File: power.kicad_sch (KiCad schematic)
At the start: 22 parts, among them IC2 MPM3833CGRH-Z, IC5 BQ24074RGTR, IC6 LP2985-30DBVR, U1 NC7SVU04P5X

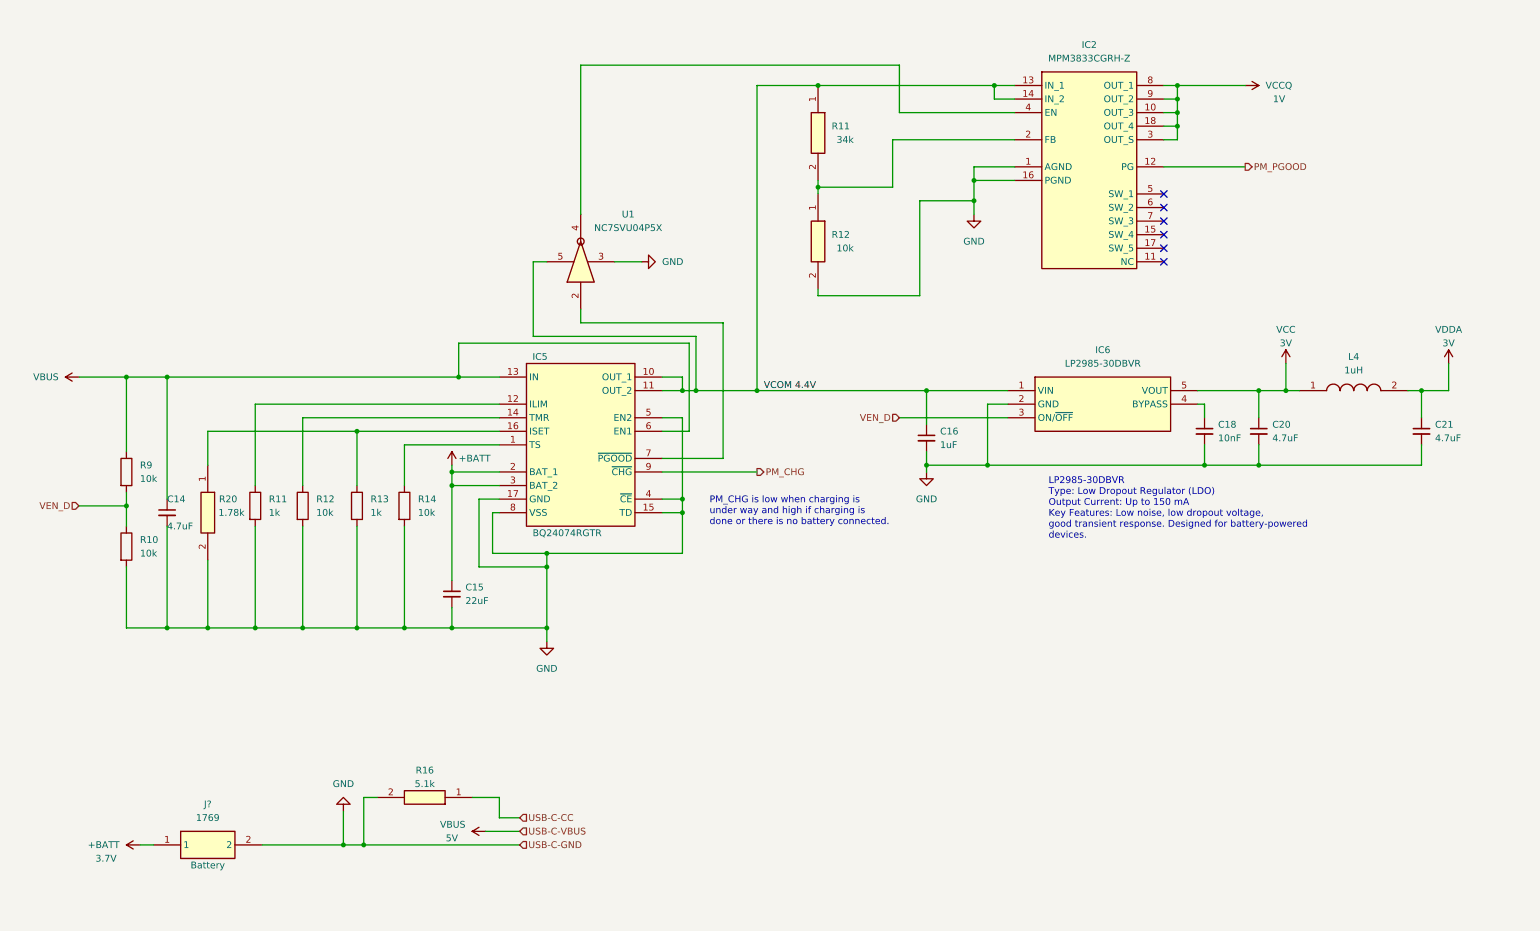
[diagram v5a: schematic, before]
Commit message: Rewired power module
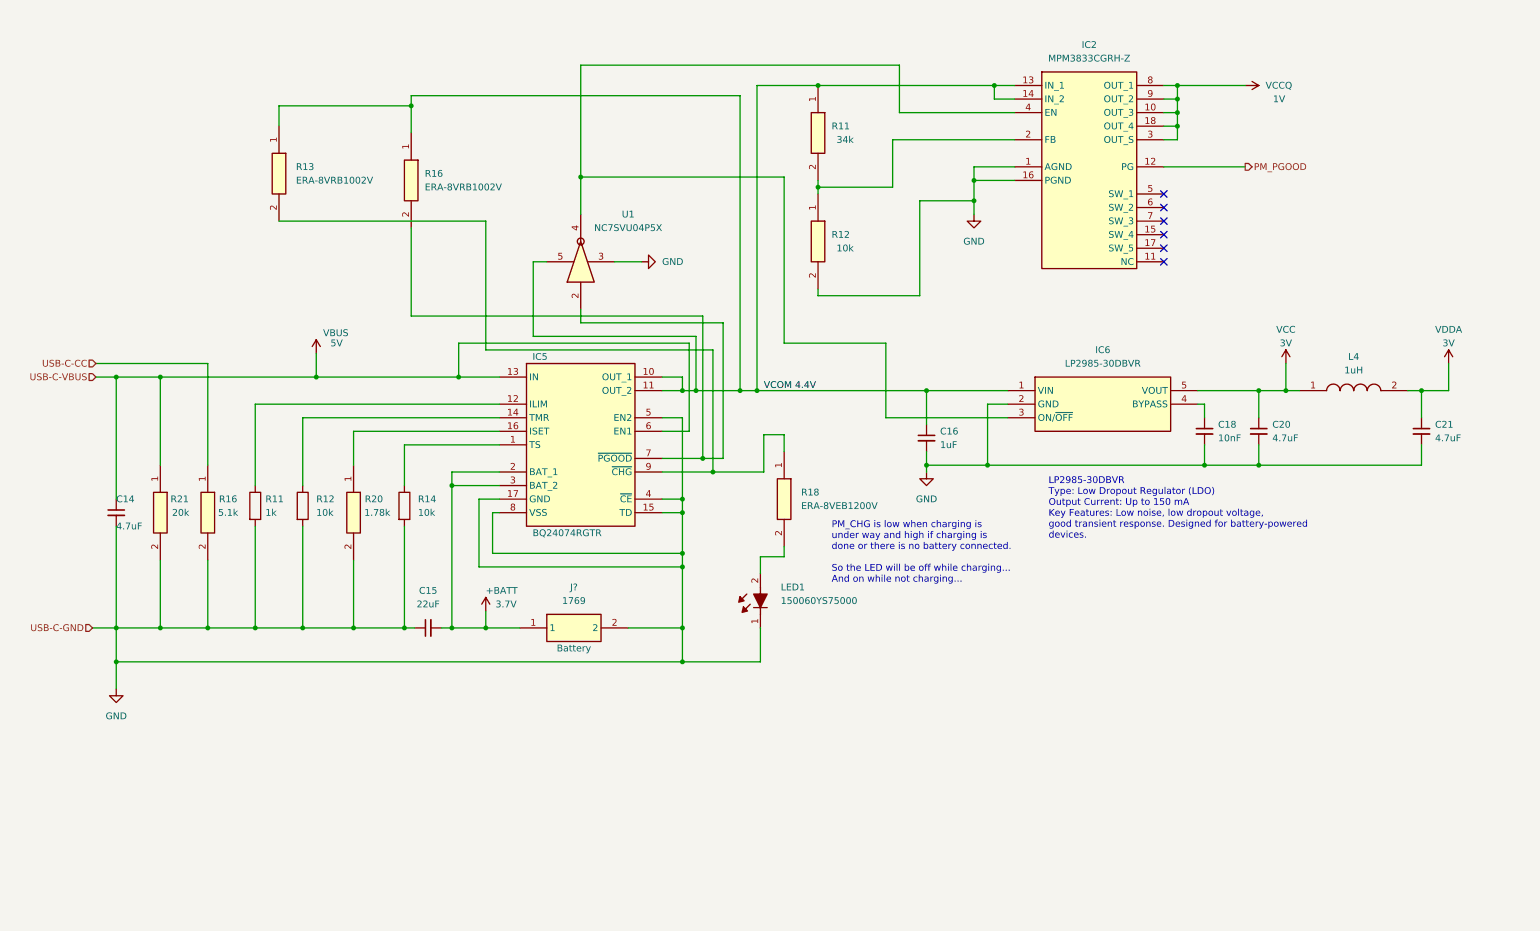
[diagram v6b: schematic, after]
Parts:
- removed R10, R9: 10k_0402, Resistor_SMD:R_0402_1005Metric, symbol PCM_4ms_Resistor:10k_0402
- removed R13: 1k_0603, 4ms_Resistor:R_0603, symbol PCM_4ms_Resistor:1k_0603
- added LED1: 150060YS75000, LEDC1608X80N, symbol SamacSys_Parts:150060YS75000
- added R13, R16: ERA-8VRB1002V, ERA8KEB1004V, symbol SamacSys_Parts:ERA-8VRB1002V
- added R18: ERA-8VEB1200V, ERA8KEB1004V, symbol SamacSys_Parts:ERA-8VEB1200V
- added R21: ERA-3VEB1781V, ERA3KV_(0603), symbol SamacSys_Parts:ERA-3VEB1781V
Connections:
- net VEN_D is gone; now on an unnamed net: IC6.3 (ON/~{OFF})
- net +BATT: now also C15.2; no longer C15.1
- net GND: now also C15.1, LED1.1 (K), R21.2; no longer C15.2
- net VBUS: now also R21.1
- net VCOM 4.4V: now also R13.1, R16.1
- net at IC5.7 (~{PGOOD}), U1.2: now also R16.2
- net PM_CHG: no longer names the net of IC5.9 (~{CHG})
- net PM_CHG: now also R13.2, R18.1
- new net: LED1.2 (A), R18.2
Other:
- note added: "PM_CHG is low when charging is under way and high if charging is done or there is no battery connected. So the LED will be off while charging... And on while not charging..."
- note removed: "PM_CHG is low when charging is under way and high if charging is done or there is no battery connected."
- moved on the sheet: C14, C15, J?, R16, R20

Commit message: Replacing global power labels with hierarchical pins
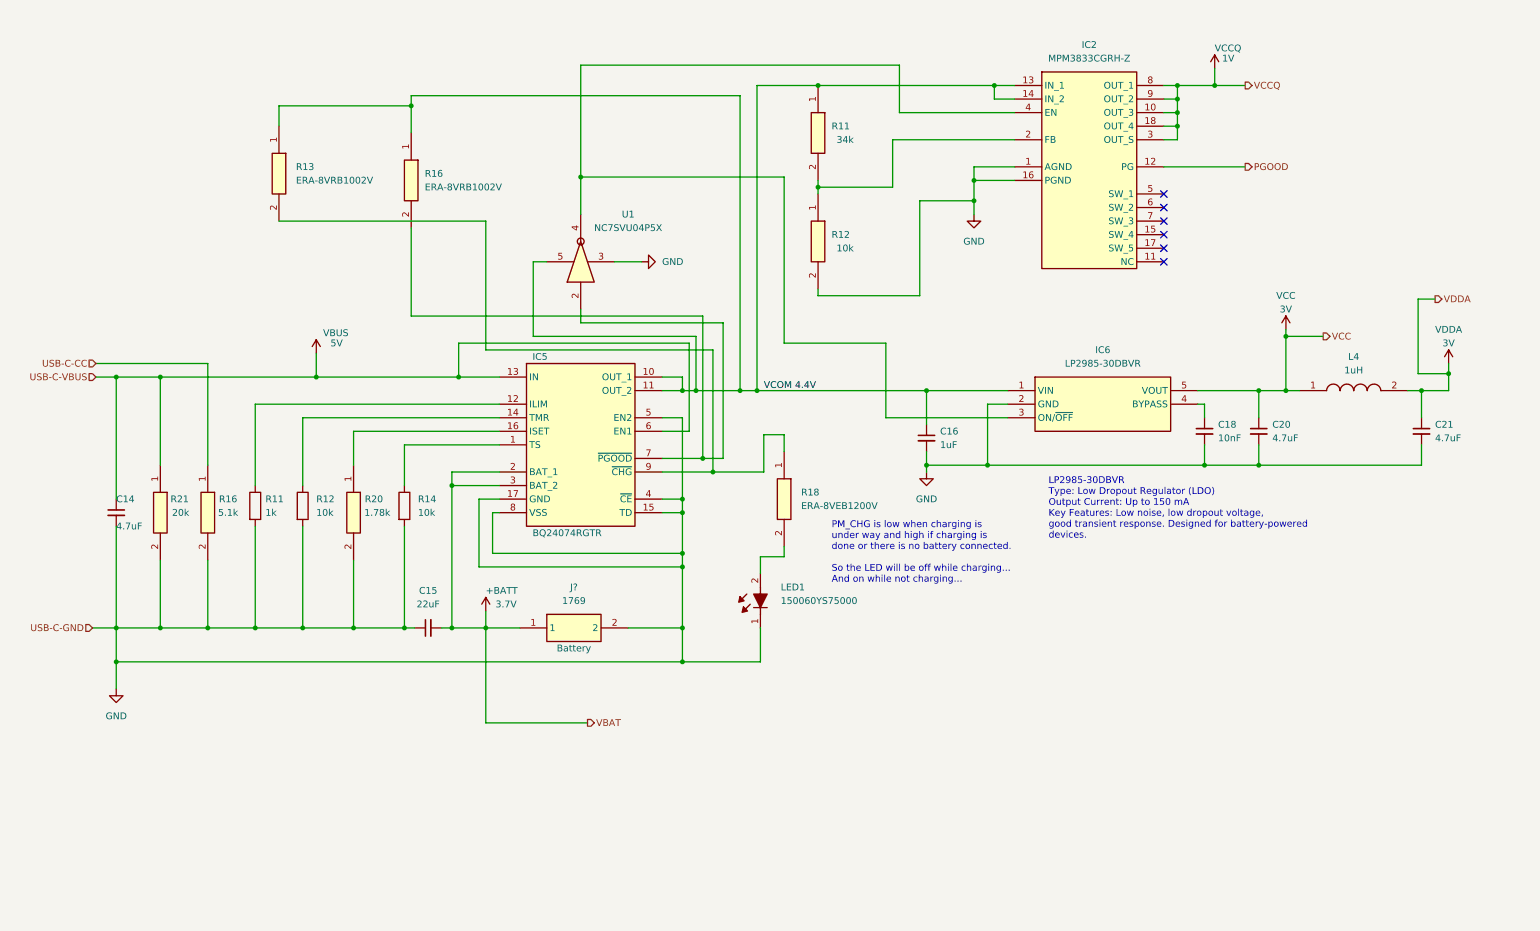
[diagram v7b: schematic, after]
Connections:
- net PM_PGOOD renamed PGOOD
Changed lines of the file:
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@@
   (junction (at 195.58 30.48) (diameter 0) (color 0 0 0 0)
   )
+  (junction (at 250.19 77.47) (diameter 0) (color 0 0 0 0)
+  )
   (junction (at 48.26 132.08) (diameter 0) (color 0 0 0 0)
   )
@@
   (junction (at 250.19 87.63) (diameter 0) (color 0 0 0 0)
   )
+  (junction (at 236.855 30.48) (diameter 0) (color 0 0 0 0)
+  )
   (junction (at 229.87 30.48) (diameter 0) (color 0 0 0 0)
   )
@@
   )
   (junction (at 229.87 35.56) (diameter 0) (color 0 0 0 0)
+  )
+  (junction (at 280.67 84.455) (diameter 0) (color 0 0 0 0)
   )
   (junction (at 151.13 87.63) (diameter 0) (color 0 0 0 0)
@@
     (stroke (width 0) (type default))
   )
+  (wire (pts (xy 274.955 70.485) (xy 274.955 84.455))
+    (stroke (width 0) (type default))
+  )
   (wire (pts (xy 31.115 132.08) (xy 31.115 138.43))
     (stroke (width 0) (type default))
@@
     (stroke (width 0) (type default))
   )
-  (wire (pts (xy 250.19 82.55) (xy 250.19 87.63))
+  (wire (pts (xy 250.19 76.2) (xy 250.19 77.47))
     (stroke (width 0) (type default))
   )
@@
     (stroke (width 0) (type default))
   )
+  (wire (pts (xy 250.19 77.47) (xy 257.175 77.47))
+    (stroke (width 0) (type default))
+  )
   (wire (pts (xy 229.87 33.02) (xy 229.87 30.48))
     (stroke (width 0) (type default))
@@
     (stroke (width 0) (type default))
   )
+  (wire (pts (xy 100.33 149.86) (xy 119.38 149.86))
+    (stroke (width 0) (type default))
+  )
   (wire (pts (xy 39.37 85.09) (xy 68.58 85.09))
     (stroke (width 0) (type default))
@@
     (stroke (width 0) (type default))
   )
+  (wire (pts (xy 236.855 30.48) (xy 242.57 30.48))
+    (stroke (width 0) (type default))
+  )
   (wire (pts (xy 68.58 80.645) (xy 68.58 85.09))
     (stroke (width 0) (type default))
@@
     (stroke (width 0) (type default))
   )
+  (wire (pts (xy 278.13 70.485) (xy 274.955 70.485))
+    (stroke (width 0) (type default))
+  )
   (wire (pts (xy 86.36 57.15) (xy 86.36 73.66))
     (stroke (width 0) (type default))
@@
     (stroke (width 0) (type default))
   )
-  (wire (pts (xy 280.67 82.55) (xy 280.67 87.63))
+  (wire (pts (xy 280.67 82.55) (xy 280.67 84.455))
     (stroke (width 0) (type default))
   )
@@
     (stroke (width 0) (type default))
   )
+  (wire (pts (xy 250.19 77.47) (xy 250.19 87.63))
+    (stroke (width 0) (type default))
+  )
   (wire (pts (xy 86.36 73.66) (xy 140.97 73.66))
     (stroke (width 0) (type default))
@@
     (stroke (width 0) (type default))
   )
+  (wire (pts (xy 100.33 132.08) (xy 100.33 149.86))
+    (stroke (width 0) (type default))
+  )
   (wire (pts (xy 273.05 87.63) (xy 275.59 87.63))
     (stroke (width 0) (type default))
@@
     (stroke (width 0) (type default))
   )
+  (wire (pts (xy 274.955 84.455) (xy 280.67 84.455))
+    (stroke (width 0) (type default))
+  )
   (wire (pts (xy 142.875 80.01) (xy 142.875 102.87))
     (stroke (width 0) (type default))
@@
     (stroke (width 0) (type default))
   )
+  (wire (pts (xy 236.855 27.305) (xy 236.855 30.48))
+    (stroke (width 0) (type default))
+  )
   (wire (pts (xy 26.67 132.08) (xy 31.115 132.08))
     (stroke (width 0) (type default))
@@
     (stroke (width 0) (type default))
   )
-  (wire (pts (xy 229.87 30.48) (xy 242.57 30.48))
+  (wire (pts (xy 229.87 30.48) (xy 236.855 30.48))
     (stroke (width 0) (type default))
   )
@@
   )
   (wire (pts (xy 118.11 74.93) (xy 144.78 74.93))
+    (stroke (width 0) (type default))
+  )
+  (wire (pts (xy 280.67 84.455) (xy 280.67 87.63))
     (stroke (width 0) (type default))
   )
@@
     (effects (font (size 1.27 1.27)) (justify right))
   )
+  (hierarchical_label "VDDA" (shape output) (at 278.13 70.485 0) (fields_autoplaced)
+    (effects (font (size 1.27 1.27)) (justify left))
+  )
+  (hierarchical_label "VBAT" (shape output) (at 119.38 149.86 0) (fields_autoplaced)
+    (effects (font (size 1.27 1.27)) (justify left))
+  )
+  (hierarchical_label "VCCQ" (shape output) (at 242.57 30.48 0) (fields_autoplaced)
+    (effects (font (size 1.27 1.27)) (justify left))
+  )
   (hierarchical_label "USB-C-VBUS" (shape input) (at 27.305 85.09 180) (fields_autoplaced)
     (effects (font (size 1.27 1.27)) (justify right))
   )
-  (hierarchical_label "PM_PGOOD" (shape output) (at 242.57 45.72 0) (fields_autoplaced)
+  (hierarchical_label "VCC" (shape output) (at 257.175 77.47 0) (fields_autoplaced)
+    (effects (font (size 1.27 1.27)) (justify left))
+  )
+  (hierarchical_label "PGOOD" (shape output) (at 242.57 45.72 0) (fields_autoplaced)
     (effects (font (size 1.27 1.27)) (justify left))
   )
@@
     )
   )
-  (symbol (lib_id "power:VCC") (at 250.19 82.55 0) (unit 1)
+  (symbol (lib_id "power:VCC") (at 250.19 76.2 0) (unit 1)
     (in_bom yes) (on_board yes) (dnp no)
-    (property "Reference" "#PWR025" (at 250.19 86.36 0)
-      (effects (font (size 1.27 1.27)) hide)
-    )
-    (property "Value" "VCC" (at 250.19 76.2 0)
-      (effects (font (size 1.27 1.27)))
-    )
-    (property "Footprint" "" (at 250.19 82.55 0)
-      (effects (font (size 1.27 1.27)) hide)
-    )
-    (property "Datasheet" "" (at 250.19 82.55 0)
-      (effects (font (size 1.27 1.27)) hide)
-    )
-    (property "Voltage" "3V" (at 250.19 78.74 0)
+    (property "Reference" "#PWR025" (at 250.19 80.01 0)
+      (effects (font (size 1.27 1.27)) hide)
+    )
+    (property "Value" "VCC" (at 250.19 69.85 0)
+      (effects (font (size 1.27 1.27)))
+    )
+    (property "Footprint" "" (at 250.19 76.2 0)
+      (effects (font (size 1.27 1.27)) hide)
+    )
+    (property "Datasheet" "" (at 250.19 76.2 0)
+      (effects (font (size 1.27 1.27)) hide)
+    )
+    (property "Voltage" "3V" (at 250.19 72.39 0)
       (effects (font (size 1.27 1.27)))
     )
@@
     )
   )
-  (symbol (lib_id "power:VCCQ") (at 242.57 30.48 270) (unit 1)
+  (symbol (lib_id "power:VCCQ") (at 236.855 27.305 0) (unit 1)
     (in_bom yes) (on_board yes) (dnp no)
-    (property "Reference" "#PWR014" (at 238.76 30.48 0)
-      (effects (font (size 1.27 1.27)) hide)
-    )
-    (property "Value" "VCCQ" (at 246.38 30.48 90)
-      (effects (font (size 1.27 1.27)) (justify left))
-    )
-    (property "Footprint" "" (at 242.57 30.48 0)
-      (effects (font (size 1.27 1.27)) hide)
-    )
-    (property "Datasheet" "" (at 242.57 30.48 0)
-      (effects (font (size 1.27 1.27)) hide)
-    )
-    (property "Voltage" "1V" (at 248.92 33.02 90)
-      (effects (font (size 1.27 1.27)))
-    )
+    (property "Reference" "#PWR014" (at 236.855 31.115 0)
+      (effects (font (size 1.27 1.27)) hide)
+    )
+    (property "Value" "VCCQ" (at 236.855 23.495 0)
+      (effects (font (size 1.27 1.27)) (justify left))
+    )
+    (property "Footprint" "" (at 236.855 27.305 0)
+      (effects (font (size 1.27 1.27)) hide)
+    )
+    (property "Datasheet" "" (at 236.855 27.305 0)
+      (effects (font (size 1.27 1.27)) hide)
+    )
+    (property "Voltage" "1V" (at 239.395 25.4 0)
+      (effects (font (size 1.27 1.27)))
+    )

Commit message: Gathering memory components
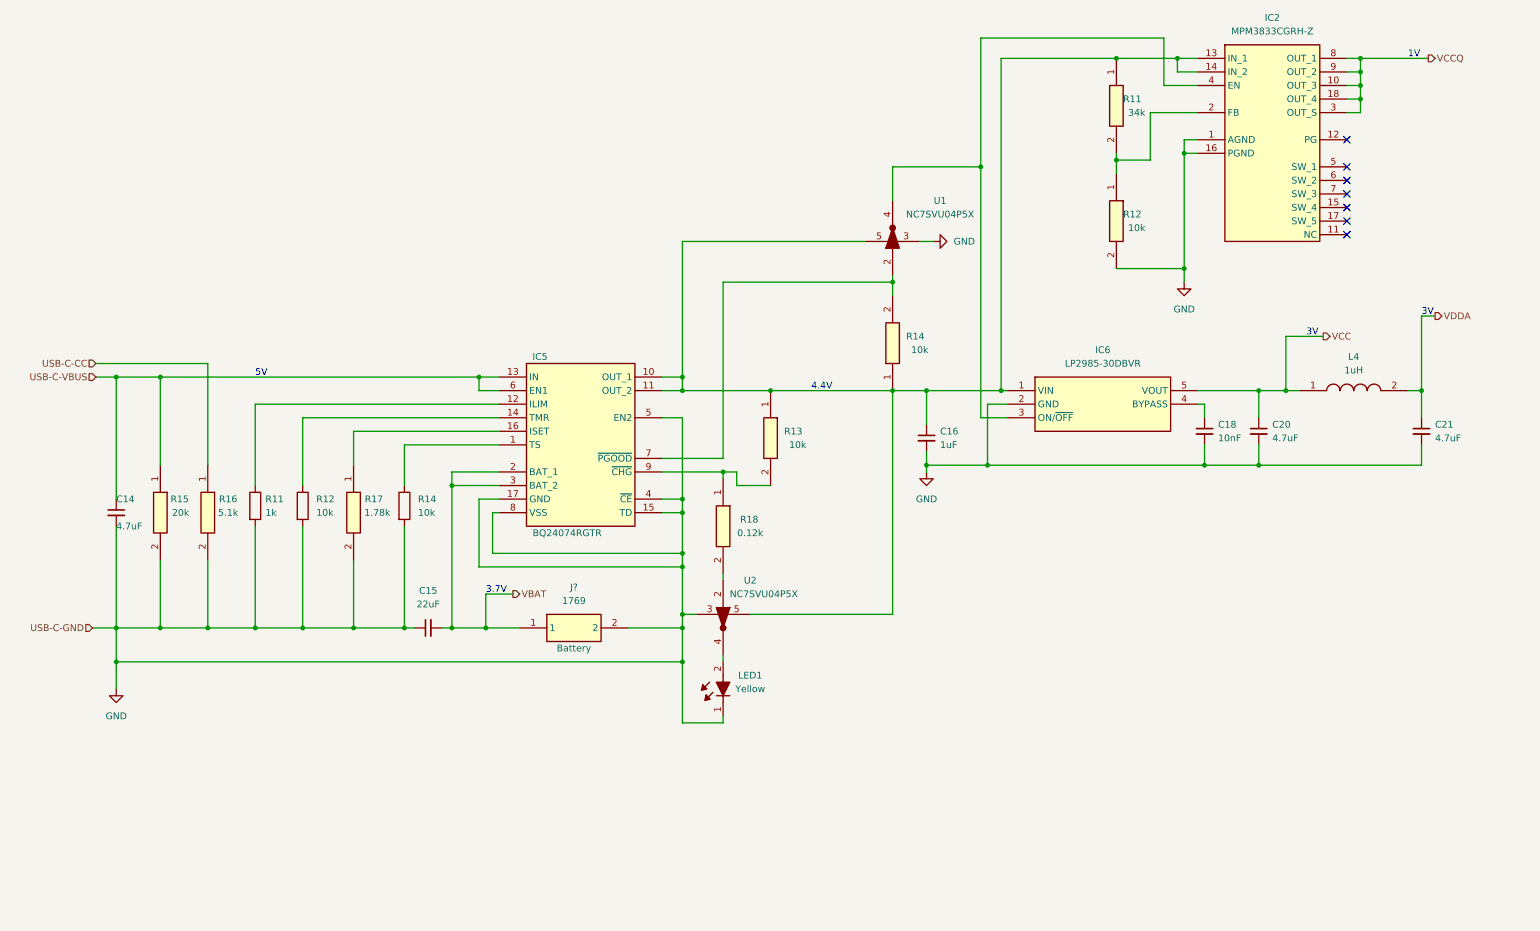
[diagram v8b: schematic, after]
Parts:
- added U2: NC7SVU04P5X, Package_TO_SOT_SMD:SOT-353_SC-70-5, symbol 74xGxx:NC7SVU04P5X
- LED1: Color (none) -> Yellow
- R13: Resistance (none) -> 10k
- R14: renamed from R16; Resistance (none) -> 10k
- R18: Resistance (none) -> 0.12k
- renumbered R21 to R15, R20 to R17
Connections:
- net GND: now also U2.3
- net at R18.2: now also U2.2; no longer LED1.2 (A)
- net +BATT renamed VBAT
- net PGOOD: no longer names the net of IC2.12 (PG)
- net VBUS renamed USB-C-VBUS
- net VCOM 4.4V: no longer names the net of C16.1, IC2.13 (IN_1), IC2.14 (IN_2), IC5.10 (OUT_1), IC5.11 (OUT_2), IC6.1 (VIN), R11.1, R13.1, R14.1, U1.5
- net VCOM 4.4V: now also U2.5
- new net: LED1.2 (A), U2.4
- no-connect marks 6 -> 7
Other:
- note added: "1V"
- note added: "3.7V"
- note added: "3V"
- note added: "4.4V"
- note added: "5V"
- note removed: "LP2985-30DBVR Type: Low Dropout Regulator (LDO) Output Current: Up to 150 mA Key Features: Low noise, low dropout voltage, good transient response. Designed for battery-powered devices."
- note removed: "PM_CHG is low when charging is under way and high if charging is done or there is no battery connected. So the LED will be off while charging... And on while not charging..."
- moved on the sheet: IC2, LED1, R11, R12, R13, R14, R18
